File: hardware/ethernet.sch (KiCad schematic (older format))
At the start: 60 parts, among them IC201 MAX5969x, IC202 KSZ8081RNA, IC203 MAX17503, J201 RJ45, J202 AUX POWER, T201 749010012A, Y201 25MHz

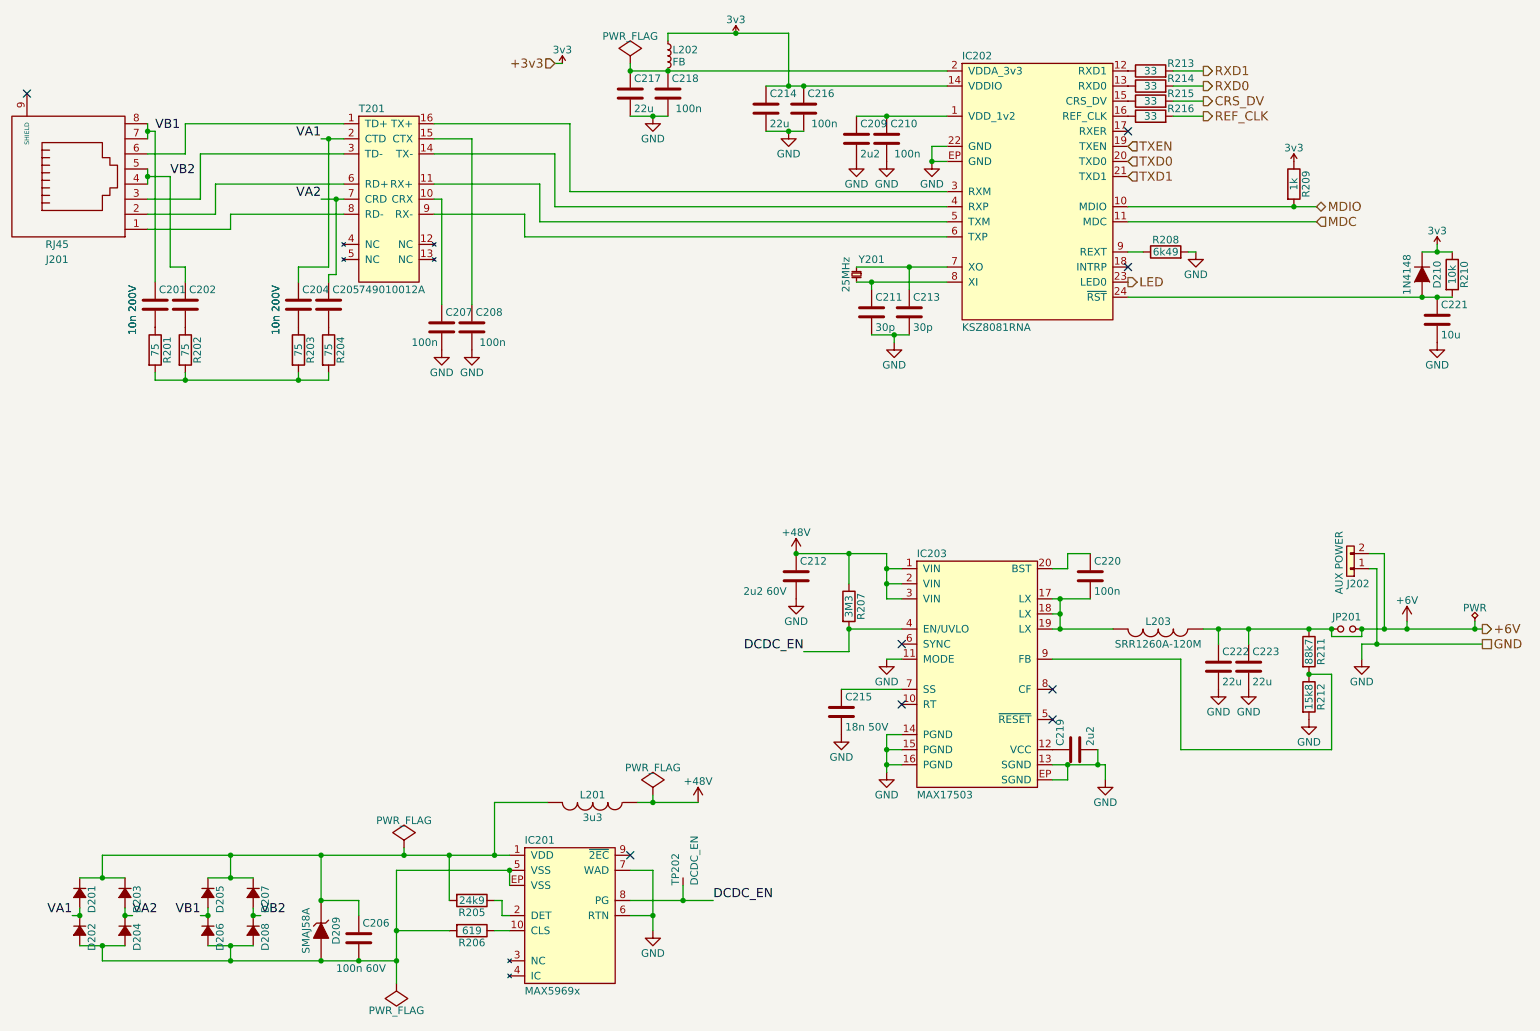
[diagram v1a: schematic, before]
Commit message: remove power schematic sheet pins
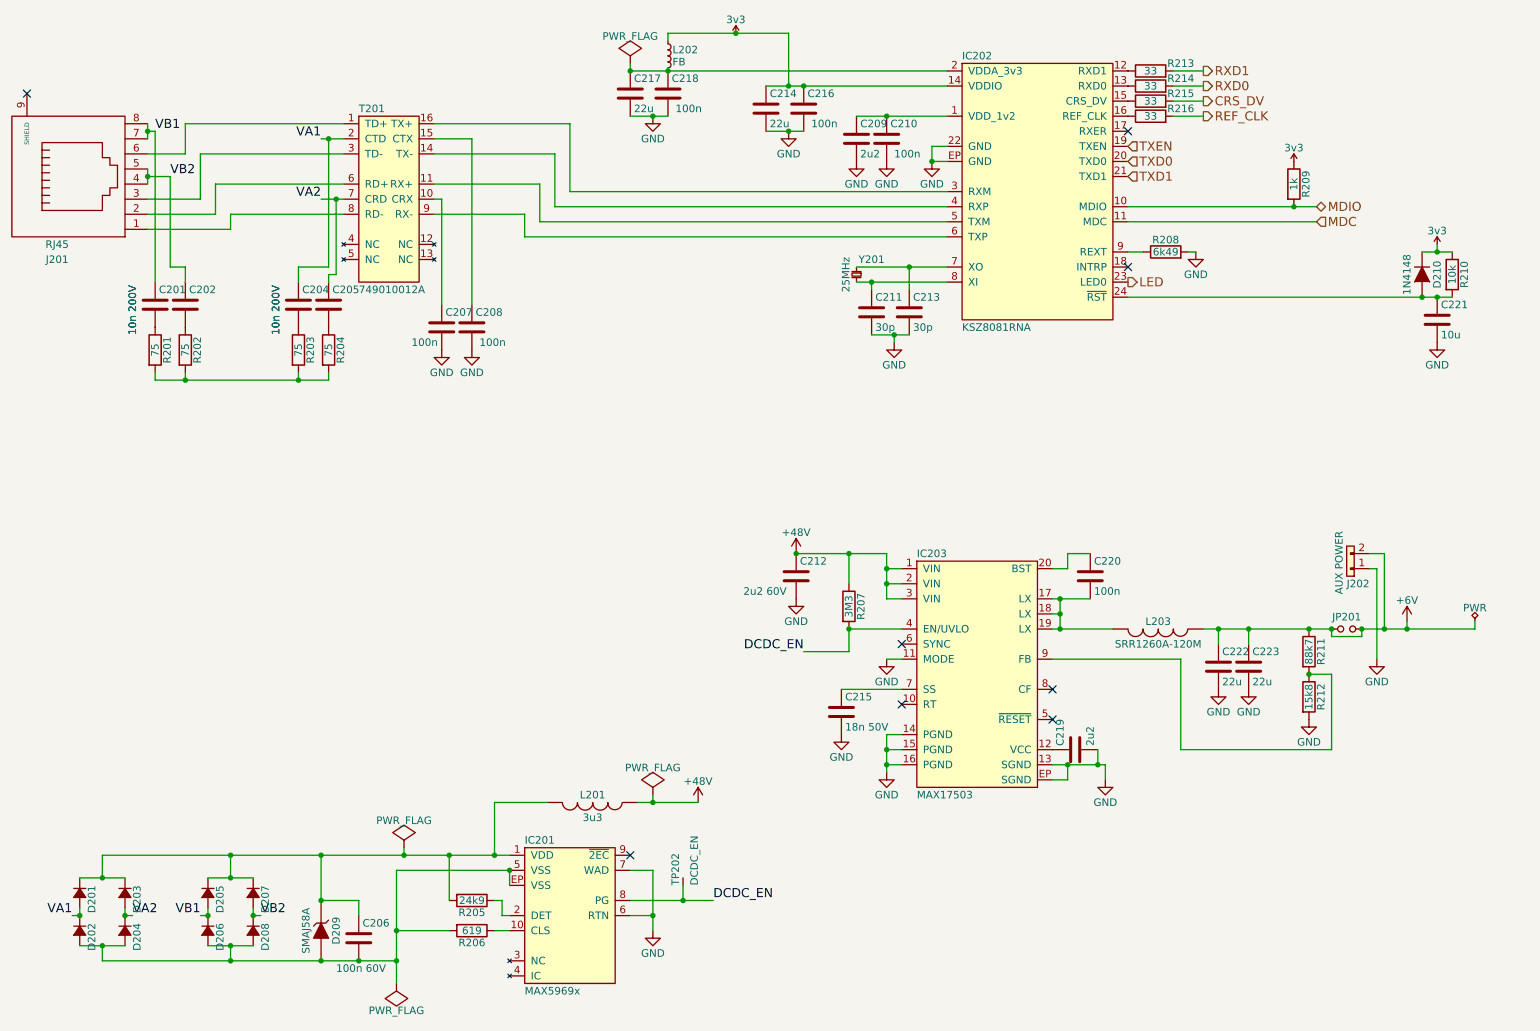
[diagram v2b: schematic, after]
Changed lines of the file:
@@
 $EndComp
 $Comp
-L +48V #PWR209
+L +48V #PWR048
 U 1 1 57F04B70
 P 5850 4100
-F 0 "#PWR209" H 5850 3950 50  0001 C CNN
+F 0 "#PWR048" H 5850 3950 50  0001 C CNN
 F 1 "+48V" H 5850 4240 50  0000 C CNN
 F 2 "" H 5850 4100 50  0000 C CNN
@@
 $EndComp
 $Comp
-L GND #PWR210
+L GND #PWR049
 U 1 1 57F04B72
 P 5850 4400
-F 0 "#PWR210" H 5850 4150 50  0001 C CNN
+F 0 "#PWR049" H 5850 4150 50  0001 C CNN
 F 1 "GND" H 5850 4250 50  0000 C CNN
 F 2 "" H 5850 4400 50  0000 C CNN
@@
 $EndComp
 $Comp
-L GND #PWR218
+L GND #PWR050
 U 1 1 57F04B74
 P 7900 5600
-F 0 "#PWR218" H 7900 5350 50  0001 C CNN
+F 0 "#PWR050" H 7900 5350 50  0001 C CNN
 F 1 "GND" H 7900 5450 50  0000 C CNN
 F 2 "" H 7900 5600 50  0000 C CNN
@@
 $EndComp
 $Comp
-L GND #PWR211
+L GND #PWR051
 U 1 1 57F04B76
 P 6150 5300
-F 0 "#PWR211" H 6150 5050 50  0001 C CNN
+F 0 "#PWR051" H 6150 5050 50  0001 C CNN
 F 1 "GND" H 6150 5150 50  0000 C CNN
 F 2 "" H 6150 5300 50  0000 C CNN
@@
 $EndComp
 $Comp
-L GND #PWR215
+L GND #PWR052
 U 1 1 57F04B77
 P 6450 5550
-F 0 "#PWR215" H 6450 5300 50  0001 C CNN
+F 0 "#PWR052" H 6450 5300 50  0001 C CNN
 F 1 "GND" H 6450 5400 50  0000 C CNN
 F 2 "" H 6450 5550 50  0000 C CNN
@@
 $EndComp
 $Comp
-L GND #PWR220
+L GND #PWR053
 U 1 1 57F04B7B
 P 8650 5000
-F 0 "#PWR220" H 8650 4750 50  0001 C CNN
+F 0 "#PWR053" H 8650 4750 50  0001 C CNN
 F 1 "GND" H 8650 4850 50  0000 C CNN
 F 2 "" H 8650 5000 50  0000 C CNN
@@
 $EndComp
 $Comp
-L +6V #PWR225
+L +6V #PWR054
 U 1 1 57F04B7C
 P 9900 4550
-F 0 "#PWR225" H 9900 4400 50  0001 C CNN
+F 0 "#PWR054" H 9900 4400 50  0001 C CNN
 F 1 "+6V" H 9900 4690 50  0000 C CNN
 F 2 "" H 9900 4550 50  0000 C CNN
@@
 $EndComp
 $Comp
-L GND #PWR223
+L GND #PWR055
 U 1 1 57F04B7F
 P 9250 5200
-F 0 "#PWR223" H 9250 4950 50  0001 C CNN
+F 0 "#PWR055" H 9250 4950 50  0001 C CNN
 F 1 "GND" H 9250 5050 50  0000 C CNN
 F 2 "" H 9250 5200 50  0000 C CNN
@@
 $EndComp
 $Comp
-L +48V #PWR206
+L +48V #PWR056
 U 1 1 57F04B83
 P 5200 5750
-F 0 "#PWR206" H 5200 5600 50  0001 C CNN
+F 0 "#PWR056" H 5200 5600 50  0001 C CNN
 F 1 "+48V" H 5200 5890 50  0000 C CNN
 F 2 "" H 5200 5750 50  0000 C CNN
@@
 $EndComp
 $Comp
-L GND #PWR205
+L GND #PWR057
 U 1 1 57F04B84
 P 4900 6600
-F 0 "#PWR205" H 4900 6350 50  0001 C CNN
+F 0 "#PWR057" H 4900 6350 50  0001 C CNN
 F 1 "GND" H 4900 6450 50  0000 C CNN
 F 2 "" H 4900 6600 50  0000 C CNN
@@
 $EndComp
 $Comp
-L GND #PWR201
+L GND #PWR058
 U 1 1 57F04B8D
 P 3500 2750
-F 0 "#PWR201" H 3500 2500 50  0001 C CNN
+F 0 "#PWR058" H 3500 2500 50  0001 C CNN
 F 1 "GND" H 3500 2600 50  0000 C CNN
 F 2 "" H 3500 2750 50  0000 C CNN
@@
 $EndComp
 $Comp
-L GND #PWR202
+L GND #PWR059
 U 1 1 57F04B8E
 P 3700 2750
-F 0 "#PWR202" H 3700 2500 50  0001 C CNN
+F 0 "#PWR059" H 3700 2500 50  0001 C CNN
 F 1 "GND" H 3700 2600 50  0000 C CNN
 F 2 "" H 3700 2750 50  0000 C CNN
@@
 $EndComp
 $Comp
-L GND #PWR221
+L GND #PWR060
 U 1 1 57F04B97
 P 8850 5000
-F 0 "#PWR221" H 8850 4750 50  0001 C CNN
+F 0 "#PWR060" H 8850 4750 50  0001 C CNN
 F 1 "GND" H 8850 4850 50  0000 C CNN
 F 2 "" H 8850 5000 50  0000 C CNN
@@
 $EndComp
 $Comp
-L GND #PWR214
+L GND #PWR061
 U 1 1 57F04B98
 P 6450 4800
-F 0 "#PWR214" H 6450 4550 50  0001 C CNN
+F 0 "#PWR061" H 6450 4550 50  0001 C CNN
 F 1 "GND" H 6450 4650 50  0000 C CNN
 F 2 "" H 6450 4800 50  0000 C CNN
@@
 	0    1    1    0
 $EndComp
-Text HLabel 10400 4600 2    60   Output ~ 0
-+6V
 Text HLabel 8550 900  2    60   Output ~ 0
 RXD1
@@
 TXD1
 $Comp
-L GND #PWR217
+L GND #PWR062
 U 1 1 57F09193
 P 6750 1500
-F 0 "#PWR217" H 6750 1250 50  0001 C CNN
+F 0 "#PWR062" H 6750 1250 50  0001 C CNN
 F 1 "GND" H 6750 1350 50  0000 C CNN
 F 2 "" H 6750 1500 50  0000 C CNN
@@
 $EndComp
 $Comp
-L GND #PWR212
+L GND #PWR063
 U 1 1 57F0CFE9
 P 6250 1500
-F 0 "#PWR212" H 6250 1250 50  0001 C CNN
+F 0 "#PWR063" H 6250 1250 50  0001 C CNN
 F 1 "GND" H 6250 1350 50  0000 C CNN
 F 2 "" H 6250 1500 50  0000 C CNN
@@
 $EndComp
 $Comp
-L GND #PWR213
+L GND #PWR064
 U 1 1 57F0D078
 P 6450 1500
-F 0 "#PWR213" H 6450 1250 50  0001 C CNN
+F 0 "#PWR064" H 6450 1250 50  0001 C CNN
 F 1 "GND" H 6450 1350 50  0000 C CNN
 F 2 "" H 6450 1500 50  0000 C CNN
@@
 $EndComp
 $Comp
-L 3v3 #PWR207
+L 3v3 #PWR065
 U 1 1 57F0D67E
 P 5450 650
-F 0 "#PWR207" H 5450 760 50  0001 L CNN
+F 0 "#PWR065" H 5450 760 50  0001 L CNN
 F 1 "3v3" H 5450 740 50  0000 C CNN
 F 2 "" H 5450 650 60  0001 C CNN
@@
 $EndComp
 $Comp
-L GND #PWR216
+L GND #PWR066
 U 1 1 57F12D2E
 P 6500 2700
-F 0 "#PWR216" H 6500 2450 50  0001 C CNN
+F 0 "#PWR066" H 6500 2450 50  0001 C CNN
 F 1 "GND" H 6500 2550 50  0000 C CNN
 F 2 "" H 6500 2700 50  0000 C CNN
@@
 $EndComp
 $Comp
-L 3v3 #PWR222
+L 3v3 #PWR067
 U 1 1 57F16B5B
 P 9150 1500
-F 0 "#PWR222" H 9150 1610 50  0001 L CNN
+F 0 "#PWR067" H 9150 1610 50  0001 L CNN
 F 1 "3v3" H 9150 1590 50  0000 C CNN
 F 2 "" H 9150 1500 60  0001 C CNN
@@
 $EndComp
 $Comp
-L GND #PWR219
+L GND #PWR068
 U 1 1 57F1933C
 P 8500 2100
-F 0 "#PWR219" H 8500 1850 50  0001 C CNN
+F 0 "#PWR068" H 8500 1850 50  0001 C CNN
 F 1 "GND" H 8500 1950 50  0000 C CNN
 F 2 "" H 8500 2100 50  0000 C CNN
@@
 $EndComp
 $Comp
-L 3v3 #PWR226
+L 3v3 #PWR069
 U 1 1 57F1DF9F
 P 10100 2050
-F 0 "#PWR226" H 10100 2160 50  0001 L CNN
+F 0 "#PWR069" H 10100 2160 50  0001 L CNN
 F 1 "3v3" H 10100 2140 50  0000 C CNN
 F 2 "" H 10100 2050 60  0001 C CNN
@@
 $EndComp
 $Comp
-L GND #PWR227
+L GND #PWR070
 U 1 1 57F1E163
 P 10100 2700
-F 0 "#PWR227" H 10100 2450 50  0001 C CNN
+F 0 "#PWR070" H 10100 2450 50  0001 C CNN
 F 1 "GND" H 10100 2550 50  0000 C CNN
 F 2 "" H 10100 2700 50  0000 C CNN
@@
 	1    0    0    -1
 $EndComp
-Text HLabel 10400 4700 2    60   UnSpc ~ 0
-GND
-$Comp
-L GND #PWR224
+$Comp
+L GND #PWR071
 U 1 1 57F26BFA
-P 9600 4800
-F 0 "#PWR224" H 9600 4550 50  0001 C CNN
-F 1 "GND" H 9600 4650 50  0000 C CNN
-F 2 "" H 9600 4800 50  0000 C CNN
-F 3 "" H 9600 4800 50  0000 C CNN
-	1    9600 4800
+P 9700 4800
+F 0 "#PWR071" H 9700 4550 50  0001 C CNN
+F 1 "GND" H 9700 4650 50  0000 C CNN
+F 2 "" H 9700 4800 50  0000 C CNN
+F 3 "" H 9700 4800 50  0000 C CNN
+	1    9700 4800
 	1    0    0    -1
 $EndComp
@@
 $EndComp
 $Comp
-L PWR #FLG205
+L PWR #FLG072
 U 1 1 57F5C8CD
 P 10350 4550
-F 0 "#FLG205" H 10350 4710 50  0001 C CNN
+F 0 "#FLG072" H 10350 4710 50  0001 C CNN
 F 1 "PWR" H 10350 4640 50  0000 C CNN
 F 2 "" H 10350 4550 50  0001 C CNN
@@
 $EndComp
 $Comp
-L GND #PWR204
+L GND #PWR073
 U 1 1 57F877E8
 P 4900 1200
-F 0 "#PWR204" H 4900 950 50  0001 C CNN
+F 0 "#PWR073" H 4900 950 50  0001 C CNN
 F 1 "GND" H 4900 1050 50  0000 C CNN
 F 2 "" H 4900 1200 50  0000 C CNN
@@
 $EndComp
 $Comp
-L GND #PWR208
+L GND #PWR074
 U 1 1 57F878B8
 P 5800 1300
-F 0 "#PWR208" H 5800 1050 50  0001 C CNN
+F 0 "#PWR074" H 5800 1050 50  0001 C CNN
 F 1 "GND" H 5800 1150 50  0000 C CNN
 F 2 "" H 5800 1300 50  0000 C CNN
@@
 	1250 6700 1250 6800
 Wire Wire Line
-	3200 6800 1250 6800
+	1250 6800 3200 6800
 Connection ~ 1250 6700
 Wire Wire Line
@@
 Connection ~ 10100 2100
 Wire Wire Line
-	9600 4700 10400 4700
-Wire Wire Line
-	9600 4700 9600 4800
+	9700 4200 9700 4800
 Wire Wire Line
 	9650 4200 9700 4200
-Wire Wire Line
-	9700 4200 9700 4700
-Connection ~ 9700 4700
-Wire Wire Line
-	9600 4600 10400 4600
 Wire Wire Line
 	9750 4600 9750 4100
@@
 Wire Wire Line
 	10350 4550 10350 4600
-Connection ~ 10350 4600
 Connection ~ 5800 1000
 Connection ~ 5000 900
@@
 $EndComp
 $Comp
-L PWR_FLAG #FLG204
+L PWR_FLAG #FLG075
 U 1 1 58004E87
 P 4900 5700
-F 0 "#FLG204" H 4900 5795 50  0001 C CNN
+F 0 "#FLG075" H 4900 5795 50  0001 C CNN
 F 1 "PWR_FLAG" H 4900 5880 50  0000 C CNN
 F 2 "" H 4900 5700 50  0000 C CNN
@@
 Connection ~ 4900 5750
 $Comp
-L PWR_FLAG #FLG202
+L PWR_FLAG #FLG076
 U 1 1 58005EDA
 P 3250 6050
-F 0 "#FLG202" H 3250 6145 50  0001 C CNN
+F 0 "#FLG076" H 3250 6145 50  0001 C CNN
 F 1 "PWR_FLAG" H 3250 6230 50  0000 C CNN
 F 2 "" H 3250 6050 50  0000 C CNN
@@
 Connection ~ 3250 6100
 $Comp
-L PWR_FLAG #FLG203
+L PWR_FLAG #FLG077
 U 1 1 5800753D
 P 4750 850
-F 0 "#FLG203" H 4750 945 50  0001 C CNN
+F 0 "#FLG077" H 4750 945 50  0001 C CNN
 F 1 "PWR_FLAG" H 4750 1030 50  0000 C CNN
 F 2 "" H 4750 850 50  0000 C CNN
@@
 	4750 850  4750 900
 Connection ~ 4750 900
-Text HLabel 4250 850  0    60   Input ~ 0
-+3v3
-$Comp
-L 3v3 #PWR203
-U 1 1 58013978
-P 4300 850
-F 0 "#PWR203" H 4300 960 50  0001 L CNN
-F 1 "3v3" H 4300 940 50  0000 C CNN
-F 2 "" H 4300 850 60  0001 C CNN
-F 3 "" H 4300 850 60  0001 C CNN
-	1    4300 850
-	1    0    0    -1
-$EndComp
-Wire Wire Line
-	4300 850  4250 850
-$Comp
-L PWR_FLAG #FLG201
+$Comp
+L PWR_FLAG #FLG078
 U 1 1 58016417
 P 3200 6950
-F 0 "#FLG201" H 3200 7045 50  0001 C CNN
+F 0 "#FLG078" H 3200 7045 50  0001 C CNN
 F 1 "PWR_FLAG" H 3200 7130 50  0000 C CNN
 F 2 "" H 3200 6950 50  0000 C CNN
@@
 Connection ~ 9600 4600
 Connection ~ 9400 4600
+Wire Wire Line
+	9600 4600 10350 4600
 $EndSCHEMATC

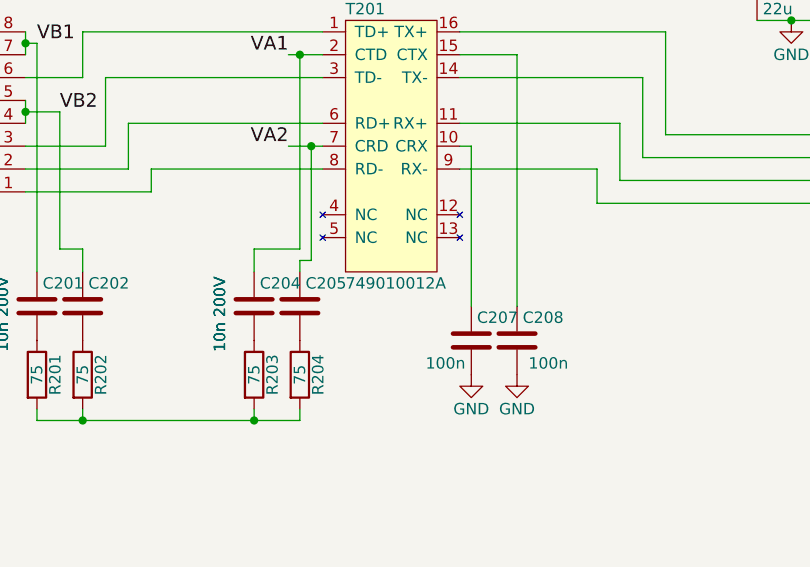
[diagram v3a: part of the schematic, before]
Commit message: Changed LAN magnetics to PoE compat part
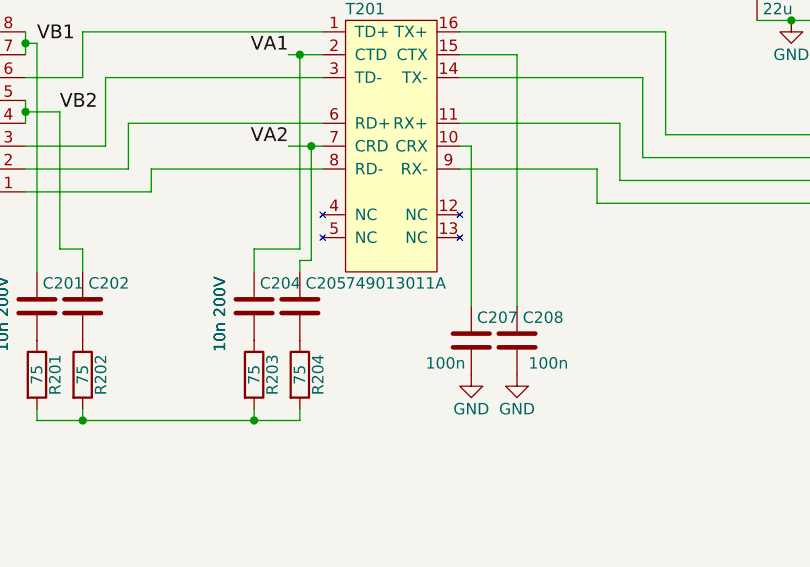
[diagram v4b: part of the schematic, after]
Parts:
- T201: value 749010012A -> 749013011A; Farnell 2422552 -> 2422553
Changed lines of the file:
@@
 P 3150 1750
 F 0 "T201" H 2950 2350 50  0000 L CNN
-F 1 "749010012A" H 2950 1150 50  0000 L CNN
+F 1 "749013011A" H 2950 1150 50  0000 L CNN
 F 2 "agg:749010012A" H 2950 1050 50  0001 L CNN
-F 3 "http://katalog.we-online.de/pbs/datasheet/749010012A.pdf" H 2950 950 50  0001 L CNN
-F 4 "2422552" H 2950 850 50  0001 L CNN "Farnell"
+F 3 "http://www.farnell.com/datasheets/1816500.pdf" H 2950 950 50  0001 L CNN
+F 4 "2422553" H 2950 850 50  0001 L CNN "Farnell"
 	1    3150 1750
 	1    0    0    -1
